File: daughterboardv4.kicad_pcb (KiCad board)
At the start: 2 copper layers, 8.6 x 10.8 mm, 8 parts, among them J1 DF30FC-24DP-0.4V_81_, U1 TXS0104EBQAR, U2 NCP170AXV180T2G

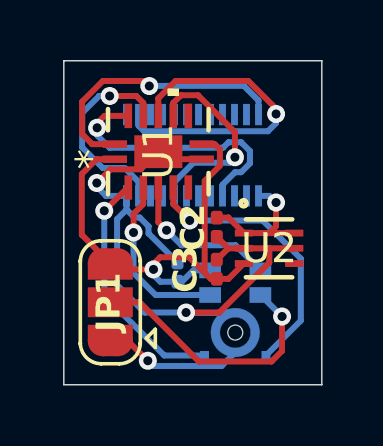
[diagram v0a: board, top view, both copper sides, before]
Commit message: Improved visibility in schematic & pcb
-Added Net Labels for signal channels on both sides of voltage shifter in Schematic Editor
-Arranged footprint silkscreen texts on the board in PCB Editor
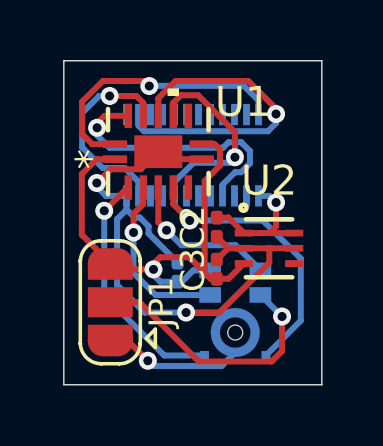
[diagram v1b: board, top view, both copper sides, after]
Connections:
- net Net-(J1-PB6) renamed /USART_TX
- net Net-(J1-PC0) renamed /DFSDM1_DATIN4
- net Net-(J1-PC1) renamed /DFSDM1_CKIN4
- net Net-(J1-PC4) renamed /INTERRUPT_EXTI4
- net Net-(MK1-CLK) renamed /MIC_CLK
- net Net-(MK1-DATA) renamed /MIC_DATA
- net Net-(MK1-THSEL) renamed /MIC_THSEL
- net Net-(MK1-WAKE) renamed /MIC_WAKE

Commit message: changed board dimension
-Change board width from 8.6mm to 8.5mm
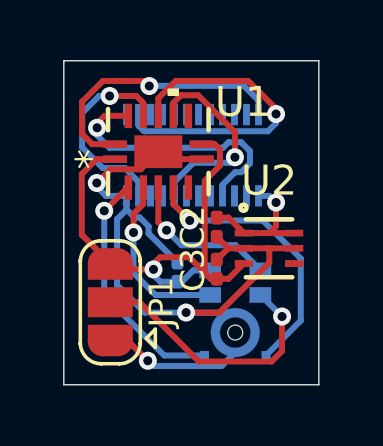
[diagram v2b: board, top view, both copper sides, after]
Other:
- board size 8.6 x 10.8 mm -> 8.5 x 10.8 mm
